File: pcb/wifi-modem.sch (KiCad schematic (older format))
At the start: 36 parts, among them J1 UART1 3V3 TTL, J2 RS232 DB9, J3 5.5X2.1MM, U1 74HC245, U2 WeMos_D1_mini, U3 MAX232, U4 SN74HC08N

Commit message: Rev 1.1
* Cleaning up schematic
* Adding missing copper void
* Added net names for RS232 signals
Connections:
- net labels added: RS232_CTS, RS232_RTS, RS232_RXD, RS232_TXD
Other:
- moved on the sheet: C1, C2, C3, C4, C5, C6, C7, D1, D2, D3, D4, D5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

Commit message: Initial commit of rev 2.0
* WeMo dev board has been deconstructed into layout
* FT232L for USB -> UART
* USB-B port for power/debug
* Native HW handshaking implementation
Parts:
- removed C7: 100n, Capacitor_THT:C_Disc_D3.8mm_W2.6mm_P2.50mm, symbol Device:C
- removed J3: 5.5X2.1MM, Connector_BarrelJack:BarrelJack_Horizontal, symbol Connector:Barrel_Jack_Switch
- removed U2: WeMos_D1_mini, Module:WEMOS_D1_mini_light, symbol MCU_Module:WeMos_D1_mini
- removed U4: SN74HC08N, Package_DIP:DIP-14_W7.62mm_Socket_LongPads, symbol michel:SN74HC08N
- added C11, C2, C5, C9: 100n, Capacitor_THT:C_Disc_D3.8mm_W2.6mm_P2.50mm, symbol Device:C
- added C14: 10n, Capacitor_THT:C_Disc_D3.8mm_W2.6mm_P2.50mm, symbol Device:C
- added C3: 100u, symbol Device:C
- added C4: 10u, symbol Device:C
- added C8: 4.7u, symbol Device:CP
- added FB1: 33 Ohms @ 100MHz, symbol Device:Ferrite_Bead_Small
- added J1: USB_B, symbol Connector:USB_B
- added Q1: BC846BDW1, Package_TO_SOT_SMD:SOT-363_SC-70-6, symbol Transistor_BJT:BC846BDW1
- added R1, R12, R13, R14, R15, R2, R3: 10k, Resistor_THT:R_Axial_DIN0204_L3.6mm_D1.6mm_P7.62mm_Horizontal, symbol Device:R_US
- added SW1: SW_Push, symbol Switch:SW_Push
- added U1: ESP-12F, RF_Module:ESP-12E, symbol RF_Module:ESP-12F
- added U3: LM1117-3.3, symbol Regulator_Linear:LM1117-3.3
- added U4: FT232RL, Package_SO:SSOP-28_5.3x10.2mm_P0.65mm, symbol Interface_USB:FT232RL
- D1: value RS (Request to Send) -> LED
- D2: value CS (Clear to Send) -> LED
- D3: value CD (Data Carrier Detect) -> LED
- D4: value RI (Ring) -> LED
- D5: value RD (Receive Data) -> LED
- D6: value SD (Send Data) -> LED
- D7: value TR (Terminal Ready) -> LED
- D8: value MR (Modem Ready) -> LED
- renumbered C4 to C10, C6 to C12, C5 to C13, C2 to C6, C3 to C7, J1 to J2, J2 to J3, R7 to R10, R8 to R11, R1 to R4, R2 to R5, R3 to R6, R4 to R7, R5 to R8, R6 to R9, U1 to U2, U3 to U5
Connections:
- net labels added: +3.3V, 3V3_TTL_RXD, 3V3_TTL_TXD, CD_LED_DRV, CTS_LED_DRV, ESP_EN, ESP_GPIO0, ESP_GPIO12, ESP_GPIO14, ESP_GPIO15_UART0_RTS, ESP_GPIO2, ESP_GPIO4, ESP_GPIO5, ESP_RST_N, ESP_UART0_CTS, ESP_UART0_RXD, ESP_UART0_TXD, FT232_3V3, FT232_CTS, FT232_DTR, FT232_RTS, FT232_RXD, FT232_TXD, MAX232_CTS, MAX232_RTS, MAX232_RXD, MAX232_TXD, MR_LED_DRV, RI_LED_DRV, RTS_LED_DRV, RX_LED_DRV, TR_LED_DRV, TX_LED_DRV, VBUS
- net labels removed: CD, CS, CS_LED, HS_DISP_CTRL, MR, RI, RS, RS_LED, RX1, RX2, RX_LED, TR, TX1, TX2, TX_LED
- wire segments 113 -> 158
- no-connect marks 7 -> 23
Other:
- note added: "0"
- note added: "1"
- note added: "All _LED_DRV are active low"
- note added: "Auto UART BL"
- note added: "CD (Data Carrier Detect)"
- note added: "CTS (Clear to Send)"
- note added: "DTR"
- note added: "ESP8266 Boot Modes"
- note added: "FLASH BOOT"
- note added: "GPIO0"
- note added: "GPIO15"
- note added: "GPIO2"
- note added: "H"
- note added: "L"
- note added: "MCU"
- note added: "MR (Modem Ready)"
- note added: "Mode"
- note added: "RI (Ring)"
- note added: "RST_N"
- note added: "RTS"
- note added: "RTS (Request to Send)"
- note added: "RXD (Receive Data)"
- note added: "Signals are inverted as we are RX/TX when WiFi/ESP is TX/RX"
- note added: "TR (Terminal Ready)"
- note added: "TXD (Transmit Data)"
- note added: "UART BL"
- note added: "USB UART"
- note added: "Will set ESP in UART BL mode for loading\nnew FW from host PC"
- note removed: "D7 is RXD2\nD8 is TXD2"
- moved on the sheet: C1, C10, C12, C13, C6, C7, D1, D2, D3, D4, D5, D6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

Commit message: Update wifi-modem.sch
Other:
- note added: "Port Pin Assignments"
- moved on the sheet: C3, C4, C9, U3
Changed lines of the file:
@@
 L Regulator_Linear:LM1117-3.3 U3
 U 1 1 5F608C6C
-P 5250 6350
-F 0 "U3" H 5250 6592 50  0000 C CNN
-F 1 "LM1117-3.3" H 5250 6501 50  0000 C CNN
-F 2 "" H 5250 6350 50  0001 C CNN
-F 3 "http://www.ti.com/lit/ds/symlink/lm1117.pdf" H 5250 6350 50  0001 C CNN
-	1    5250 6350
+P 4800 6300
+F 0 "U3" H 4800 6542 50  0000 C CNN
+F 1 "LM1117-3.3" H 4800 6451 50  0000 C CNN
+F 2 "" H 4800 6300 50  0001 C CNN
+F 3 "http://www.ti.com/lit/ds/symlink/lm1117.pdf" H 4800 6300 50  0001 C CNN
+	1    4800 6300
 	-1   0    0    -1
 $EndComp
@@
 L Device:C C4
 U 1 1 5F71DBDE
-P 5700 6600
-F 0 "C4" H 5815 6646 50  0000 L CNN
-F 1 "10u" H 5815 6555 50  0000 L CNN
-F 2 "" H 5738 6450 50  0001 C CNN
-F 3 "~" H 5700 6600 50  0001 C CNN
-	1    5700 6600
+P 5250 6550
+F 0 "C4" H 5365 6596 50  0000 L CNN
+F 1 "10u" H 5365 6505 50  0000 L CNN
+F 2 "" H 5288 6400 50  0001 C CNN
+F 3 "~" H 5250 6550 50  0001 C CNN
+	1    5250 6550
 	1    0    0    -1
 $EndComp
@@
 L Device:C C3
 U 1 1 5F71EAE8
-P 4800 6600
-F 0 "C3" H 4915 6646 50  0000 L CNN
-F 1 "100u" H 4915 6555 50  0000 L CNN
-F 2 "" H 4838 6450 50  0001 C CNN
-F 3 "~" H 4800 6600 50  0001 C CNN
-	1    4800 6600
+P 4350 6550
+F 0 "C3" H 4465 6596 50  0000 L CNN
+F 1 "100u" H 4465 6505 50  0000 L CNN
+F 2 "" H 4388 6400 50  0001 C CNN
+F 3 "~" H 4350 6550 50  0001 C CNN
+	1    4350 6550
 	1    0    0    -1
 $EndComp
@@
 L power:GND #PWR014
 U 1 1 5F71F8C2
-P 4800 6850
-F 0 "#PWR014" H 4800 6600 50  0001 C CNN
-F 1 "GND" H 4805 6677 50  0000 C CNN
-F 2 "" H 4800 6850 50  0001 C CNN
-F 3 "" H 4800 6850 50  0001 C CNN
-	1    4800 6850
+P 4350 6800
+F 0 "#PWR014" H 4350 6550 50  0001 C CNN
+F 1 "GND" H 4355 6627 50  0000 C CNN
+F 2 "" H 4350 6800 50  0001 C CNN
+F 3 "" H 4350 6800 50  0001 C CNN
+	1    4350 6800
 	1    0    0    -1
 $EndComp
@@
 L power:GND #PWR015
 U 1 1 5F72055C
-P 5250 6850
-F 0 "#PWR015" H 5250 6600 50  0001 C CNN
-F 1 "GND" H 5255 6677 50  0000 C CNN
-F 2 "" H 5250 6850 50  0001 C CNN
-F 3 "" H 5250 6850 50  0001 C CNN
-	1    5250 6850
+P 4800 6800
+F 0 "#PWR015" H 4800 6550 50  0001 C CNN
+F 1 "GND" H 4805 6627 50  0000 C CNN
+F 2 "" H 4800 6800 50  0001 C CNN
+F 3 "" H 4800 6800 50  0001 C CNN
+	1    4800 6800
 	1    0    0    -1
 $EndComp
@@
 L power:GND #PWR017
 U 1 1 5F720945
-P 5700 6850
-F 0 "#PWR017" H 5700 6600 50  0001 C CNN
-F 1 "GND" H 5705 6677 50  0000 C CNN
-F 2 "" H 5700 6850 50  0001 C CNN
-F 3 "" H 5700 6850 50  0001 C CNN
-	1    5700 6850
-	1    0    0    -1
-$EndComp
-Wire Wire Line
-	4800 6750 4800 6850
-Wire Wire Line
-	5250 6650 5250 6850
-Wire Wire Line
-	5700 6750 5700 6850
-Wire Wire Line
-	4800 6450 4800 6350
-Wire Wire Line
-	4800 6350 4950 6350
-Wire Wire Line
-	5550 6350 5700 6350
-Wire Wire Line
-	5700 6350 5700 6450
+P 5250 6800
+F 0 "#PWR017" H 5250 6550 50  0001 C CNN
+F 1 "GND" H 5255 6627 50  0000 C CNN
+F 2 "" H 5250 6800 50  0001 C CNN
+F 3 "" H 5250 6800 50  0001 C CNN
+	1    5250 6800
+	1    0    0    -1
+$EndComp
+Wire Wire Line
+	4350 6700 4350 6800
+Wire Wire Line
+	4800 6600 4800 6800
+Wire Wire Line
+	5250 6700 5250 6800
+Wire Wire Line
+	4350 6400 4350 6300
+Wire Wire Line
+	4350 6300 4500 6300
+Wire Wire Line
+	5100 6300 5250 6300
+Wire Wire Line
+	5250 6300 5250 6400
 $Comp
 L power:+5V #PWR016
 U 1 1 5F731B33
-P 5700 6250
-F 0 "#PWR016" H 5700 6100 50  0001 C CNN
-F 1 "+5V" H 5715 6423 50  0000 C CNN
-F 2 "" H 5700 6250 50  0001 C CNN
-F 3 "" H 5700 6250 50  0001 C CNN
-	1    5700 6250
+P 5250 6200
+F 0 "#PWR016" H 5250 6050 50  0001 C CNN
+F 1 "+5V" H 5265 6373 50  0000 C CNN
+F 2 "" H 5250 6200 50  0001 C CNN
+F 3 "" H 5250 6200 50  0001 C CNN
+	1    5250 6200
 	1    0    0    -1
 $EndComp
@@
 L power:+3.3V #PWR013
 U 1 1 5F73618C
-P 4800 6250
-F 0 "#PWR013" H 4800 6100 50  0001 C CNN
-F 1 "+3.3V" H 4815 6423 50  0000 C CNN
-F 2 "" H 4800 6250 50  0001 C CNN
-F 3 "" H 4800 6250 50  0001 C CNN
-	1    4800 6250
-	1    0    0    -1
-$EndComp
-Wire Wire Line
-	4800 6250 4800 6350
-Connection ~ 4800 6350
-Wire Wire Line
-	5700 6250 5700 6350
-Connection ~ 5700 6350
+P 4350 6200
+F 0 "#PWR013" H 4350 6050 50  0001 C CNN
+F 1 "+3.3V" H 4365 6373 50  0000 C CNN
+F 2 "" H 4350 6200 50  0001 C CNN
+F 3 "" H 4350 6200 50  0001 C CNN
+	1    4350 6200
+	1    0    0    -1
+$EndComp
+Wire Wire Line
+	4350 6200 4350 6300
+Connection ~ 4350 6300
+Wire Wire Line
+	5250 6200 5250 6300
+Connection ~ 5250 6300
 Text GLabel 4650 1500 2    50   Input ~ 0
 ESP_UART0_TXD
@@
 Wire Wire Line
 	4050 2800 4050 2700
-Text Notes 5450 5500 0    50   ~ 10
+Text Notes 5550 5600 0    50   ~ 10
 Auto UART BL
 $Comp
@@
 Wire Wire Line
 	3100 2000 3100 2050
-Text Notes 3700 3250 0    50   ~ 10
+Text Notes 3350 3250 0    50   ~ 10
 ESP8266 Boot Modes
 Wire Notes Line
@@
 Wire Notes Line
 	3300 3300 4900 3300
-Text GLabel 9650 2800 0    50   Input ~ 0
+Text GLabel 9500 2850 0    50   Input ~ 0
 ESP_UART0_RXD
-Text GLabel 9650 2900 0    50   Input ~ 0
+Text GLabel 9500 2950 0    50   Input ~ 0
 ESP_UART0_TXD
 Wire Wire Line
-	9650 2800 9750 2800
-Wire Wire Line
-	9750 2900 9650 2900
+	9500 2850 9600 2850
+Wire Wire Line
+	9600 2950 9500 2950
 $Comp
 L power:+5V #PWR020
@@
 L Device:C C9
 U 1 1 5FB63B3E
-P 8500 2400
-F 0 "C9" H 8615 2446 50  0000 L CNN
-F 1 "100n" H 8615 2355 50  0000 L CNN
-F 2 "Capacitor_THT:C_Disc_D3.8mm_W2.6mm_P2.50mm" H 8538 2250 50  0001 C CNN
-F 3 "~" H 8500 2400 50  0001 C CNN
-	1    8500 2400
+P 8500 2150
+F 0 "C9" H 8615 2196 50  0000 L CNN
+F 1 "100n" H 8615 2105 50  0000 L CNN
+F 2 "Capacitor_THT:C_Disc_D3.8mm_W2.6mm_P2.50mm" H 8538 2000 50  0001 C CNN
+F 3 "~" H 8500 2150 50  0001 C CNN
+	1    8500 2150
 	1    0    0    -1
 $EndComp
@@
 Text GLabel 7800 1400 2    50   Input ~ 0
 FT232_3V3
-Text GLabel 8400 2200 0    50   Input ~ 0
+Text GLabel 8400 1950 0    50   Input ~ 0
 FT232_3V3
 Wire Wire Line
-	8400 2200 8500 2200
-Wire Wire Line
-	8500 2200 8500 2250
+	8400 1950 8500 1950
+Wire Wire Line
+	8500 1950 8500 2000
 $Comp
 L power:GND #PWR029
 U 1 1 5FB9B45B
-P 8500 2600
-F 0 "#PWR029" H 8500 2350 50  0001 C CNN
-F 1 "GND" H 8505 2427 50  0000 C CNN
-F 2 "" H 8500 2600 50  0001 C CNN
-F 3 "" H 8500 2600 50  0001 C CNN
-	1    8500 2600
-	1    0    0    -1
-$EndComp
-Wire Wire Line
-	8500 2550 8500 2600
+P 8500 2350
+F 0 "#PWR029" H 8500 2100 50  0001 C CNN
+F 1 "GND" H 8505 2177 50  0000 C CNN
+F 2 "" H 8500 2350 50  0001 C CNN
+F 3 "" H 8500 2350 50  0001 C CNN
+	1    8500 2350
+	1    0    0    -1
+$EndComp
+Wire Wire Line
+	8500 2300 8500 2350
 NoConn ~ 7800 2500
 NoConn ~ 7800 2300
 NoConn ~ 7800 2100
-Text GLabel 9750 2800 2    50   Input ~ 0
+Text GLabel 9600 2850 2    50   Input ~ 0
 FT232_TXD
-Text GLabel 9750 2900 2    50   Input ~ 0
+Text GLabel 9600 2950 2    50   Input ~ 0
 FT232_RXD
 Text GLabel 6200 1400 0    50   Input ~ 0
@@
 Wire Wire Line
 	9800 1150 9800 1500
-Wire Notes Line
-	2600 4050 2600 5600
-Wire Notes Line
-	6150 5600 6150 4050
-Text GLabel 9650 3300 0    50   Input ~ 0
+Text GLabel 9500 3350 0    50   Input ~ 0
 ESP_UART0_RXD
-Text GLabel 9650 3400 0    50   Input ~ 0
+Text GLabel 9500 3450 0    50   Input ~ 0
 ESP_UART0_TXD
-Text GLabel 9650 3500 0    50   Input ~ 0
+Text GLabel 9500 3550 0    50   Input ~ 0
 ESP_UART0_CTS
-Text GLabel 9750 3300 2    50   Input ~ 0
+Text GLabel 9600 3350 2    50   Input ~ 0
 MAX232_TXD
-Text GLabel 9750 3400 2    50   Input ~ 0
+Text GLabel 9600 3450 2    50   Input ~ 0
 MAX232_RXD
-Text GLabel 9750 3500 2    50   Input ~ 0
+Text GLabel 9600 3550 2    50   Input ~ 0
 MAX232_RTS
-Text GLabel 9750 3600 2    50   Input ~ 0
+Text GLabel 9600 3650 2    50   Input ~ 0
 MAX232_CTS
 Wire Wire Line
-	9650 3300 9750 3300
-Wire Wire Line
-	9750 3400 9650 3400
-Wire Wire Line
-	9650 3500 9750 3500
-Wire Wire Line
-	9750 3600 9650 3600
+	9500 3350 9600 3350
+Wire Wire Line
+	9600 3450 9500 3450
+Wire Wire Line
+	9500 3550 9600 3550
+Wire Wire Line
+	9600 3650 9500 3650
 Text GLabel 6800 5300 0    50   Input ~ 0
 MAX232_TXD
@@
 Text GLabel 6200 1600 0    50   Input ~ 0
 FT232_RTS
-Text GLabel 9650 3000 0    50   Input ~ 0
+Text GLabel 9500 3050 0    50   Input ~ 0
 ESP_UART0_CTS
 Wire Wire Line
-	9650 3000 9750 3000
-Wire Wire Line
-	9750 3100 9650 3100
-Text GLabel 9750 3000 2    50   Input ~ 0
+	9500 3050 9600 3050
+Wire Wire Line
+	9600 3150 9500 3150
+Text GLabel 9600 3050 2    50   Input ~ 0
 FT232_RTS
-Text GLabel 9750 3100 2    50   Input ~ 0
+Text GLabel 9600 3150 2    50   Input ~ 0
 FT232_CTS
-Text GLabel 9650 3100 0    50   Input ~ 0
+Text GLabel 9500 3150 0    50   Input ~ 0
 ESP_GPIO15_UART0_RTS
-Text GLabel 9650 3600 0    50   Input ~ 0
+Text GLabel 9500 3650 0    50   Input ~ 0
 ESP_GPIO15_UART0_RTS
 Text GLabel 6200 1800 0    50   Input ~ 0
@@
 Wire Notes Line
 	3200 5850 3450 5850
-Text GLabel 9750 3800 2    50   Input ~ 0
+Text GLabel 9600 3850 2    50   Input ~ 0
 3V3_TTL_TXD
-Text GLabel 9750 3900 2    50   Input ~ 0
+Text GLabel 9600 3950 2    50   Input ~ 0
 3V3_TTL_RXD
-Text GLabel 9650 3900 0    50   Input ~ 0
+Text GLabel 9500 3950 0    50   Input ~ 0
 ESP_UART0_RXD
-Text GLabel 9650 3800 0    50   Input ~ 0
+Text GLabel 9500 3850 0    50   Input ~ 0
 ESP_UART0_TXD
 Wire Wire Line
-	9650 3800 9750 3800
-Wire Wire Line
-	9750 3900 9650 3900
+	9500 3850 9600 3850
+Wire Wire Line
+	9600 3950 9500 3950
 $Comp
 L Device:C C5
@@
 	2600 4050 6150 4050
 Wire Notes Line
-	2600 5600 6150 5600
+	2600 5650 6150 5650
 Wire Notes Line
 	4700 4550 4700 5150
@@
 Wire Wire Line
 	850  2000 1650 2000
+Wire Notes Line
+	10200 2600 8050 2600
+Wire Notes Line
+	8050 4050 10200 4050
+Text Notes 8100 2700 0    50   ~ 10
+Port Pin Assignments
+Wire Notes Line
+	8050 2600 8050 4050
+Wire Notes Line
+	10200 2600 10200 4050
+Wire Notes Line
+	8050 2750 10200 2750
+Wire Notes Line
+	2600 4050 2600 5650
+Wire Notes Line
+	6150 4050 6150 5650
+Wire Notes Line
+	6150 5500 2600 5500
 $EndSCHEMATC

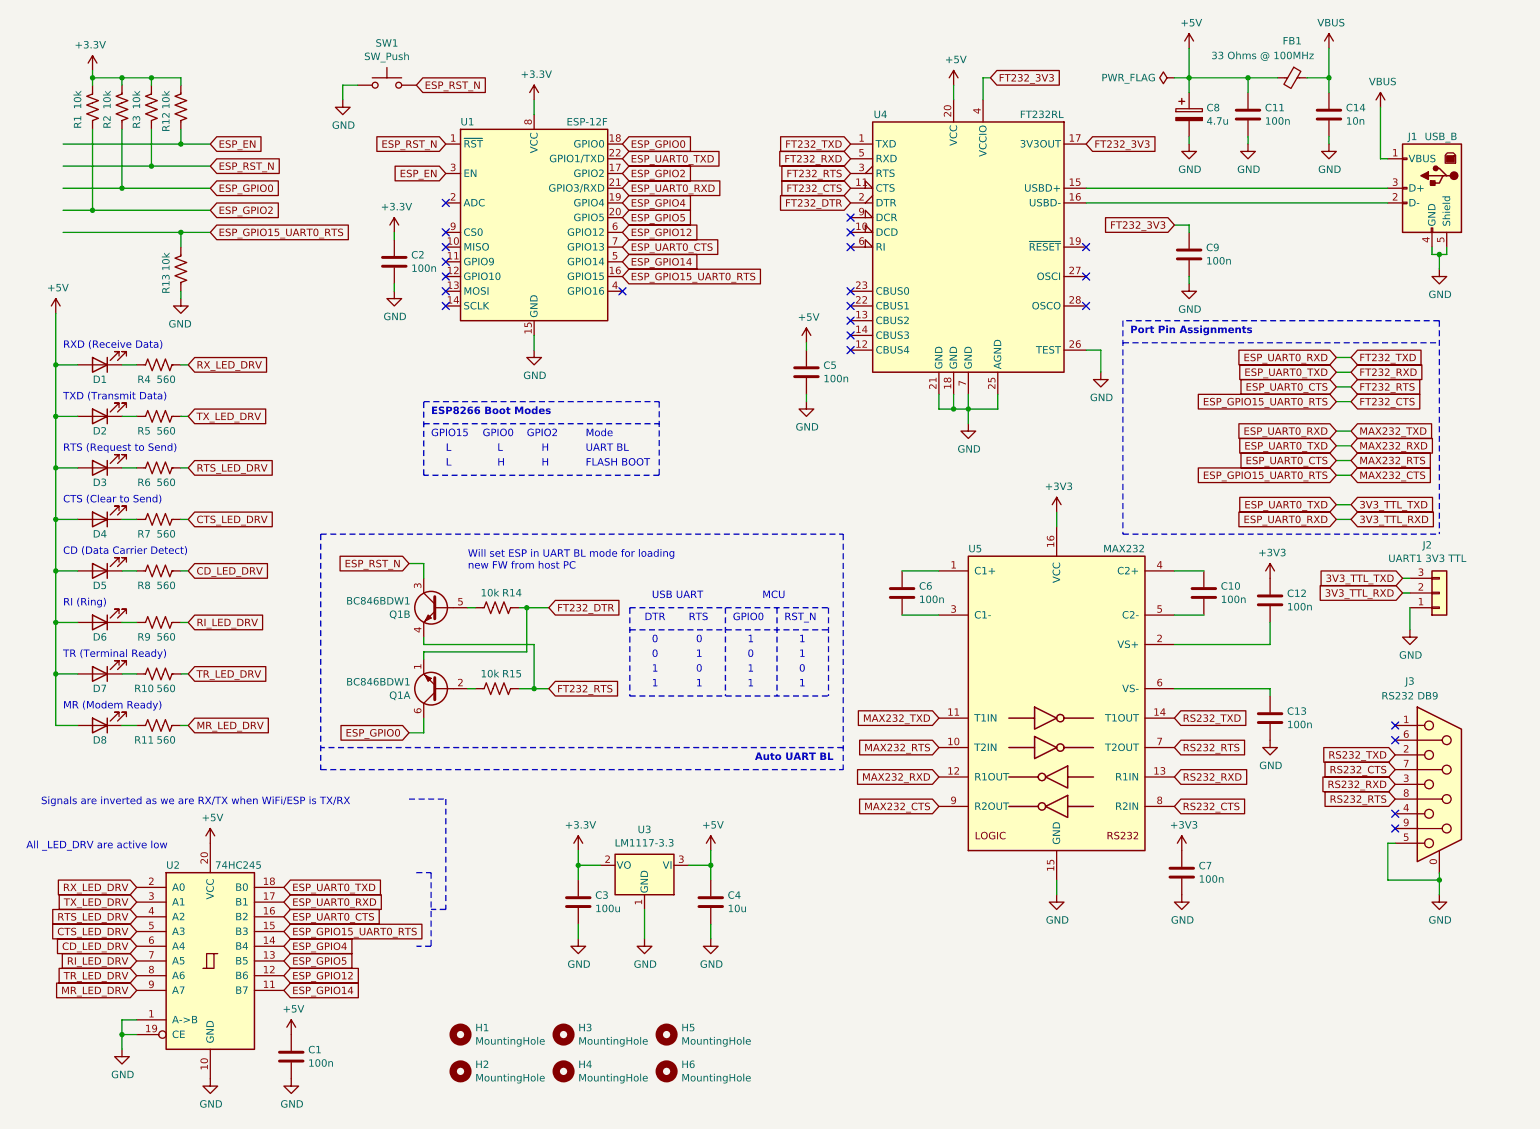
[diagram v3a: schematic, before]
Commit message: PCB layout + footprint changes
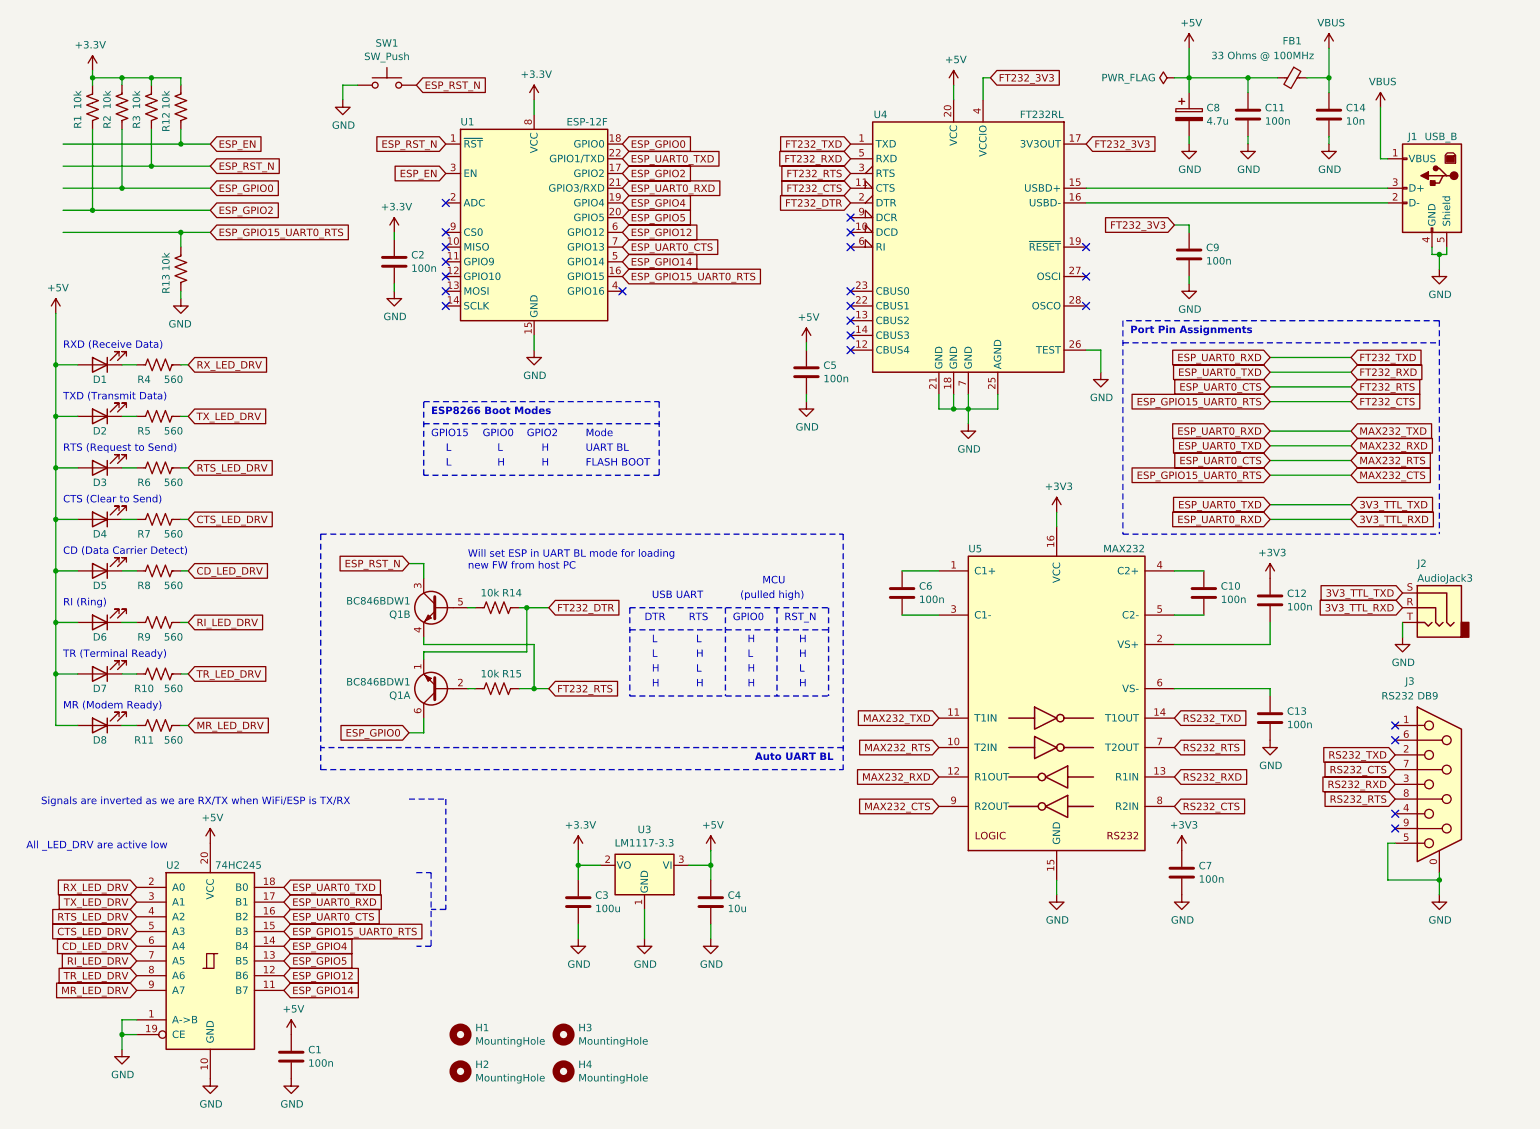
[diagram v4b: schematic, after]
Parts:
- removed H5, H6: MountingHole, MountingHole:MountingHole_3.2mm_M3, symbol Mechanical:MountingHole
- removed J2: UART1 3V3 TTL, Connector_PinSocket_2.54mm:PinSocket_1x03_P2.54mm_Horizontal, symbol Connector_Generic:Conn_01x03
- added J2: AudioJack3, Connector_Audio:Jack_3.5mm_CUI_SJ1-3533NG_Horizontal_CircularHoles, symbol Connector:AudioJack3
- C1, C10, C11, C12, C13, C14, C2, C5, C6, C7, C9: footprint Capacitor_THT:C_Disc_D3.8mm_W2.6mm_P2.50mm -> Capacitor_SMD:C_0805_2012Metric_Pad1.15x1.40mm_HandSolder
- C3, C4: footprint (none) -> Capacitor_SMD:C_0805_2012Metric_Pad1.15x1.40mm_HandSolder
- C8: footprint (none) -> Capacitor_Tantalum_SMD:CP_EIA-3216-18_Kemet-A_Pad1.58x1.35mm_HandSolder
- FB1: footprint (none) -> Inductor_SMD:L_0805_2012Metric_Pad1.15x1.40mm_HandSolder
- J1: footprint (none) -> Connector_USB:USB_B_OST_USB-B1HSxx_Horizontal
- R1, R10, R11, R12, R13, R14, R15, R2, R3, R4, R5, R6, R7, R8, R9: footprint Resistor_THT:R_Axial_DIN0204_L3.6mm_D1.6mm_P7.62mm_Horizontal -> Resistor_SMD:R_0805_2012Metric_Pad1.15x1.40mm_HandSolder
- SW1: footprint (none) -> Button_Switch_SMD:SW_SPST_PTS645
- U2: footprint Package_DIP:DIP-20_W7.62mm_Socket_LongPads -> Package_SO:SOIC-20W_7.5x12.8mm_P1.27mm
- U3: footprint (none) -> Package_TO_SOT_SMD:SOT-223-3_TabPin2
- U5: footprint Package_DIP:DIP-16_W7.62mm_Socket_LongPads -> Package_SO:SOIC-16W_7.5x10.3mm_P1.27mm
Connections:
- wire segments 158 -> 156
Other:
- note added: "(pulled high)"
- note removed: "0"
- note removed: "1"
